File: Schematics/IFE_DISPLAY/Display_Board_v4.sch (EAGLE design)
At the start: 38 parts, among them J1 POWER_JACKPTH

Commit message: Display v4 - Routing
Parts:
- added R11, R4, R6: 23k, rcl:R-US_R0603
- added U$12: MC34063AD, Display_Custom:MC34063AD
- J1: value POWER_JACKPTH -> 5.5x2.1mm Barrel; device SparkFun-Connectors:POWER_JACKPTH -> SparkFun-Connectors:POWER_JACKSMD
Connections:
- net ~CS_CAN renamed !CS_CAN
- net ~INT_CAN renamed !INT_CAN
- new net !A_CS: ATMEGA328P.PD5, U$7.LOAD/CSN
- new net !B_CS: ATMEGA328P.PD4, U$8.LOAD/CSN
- new net !C_CS: ATMEGA328P.PD3, U$9.LOAD/CSN
- new net A_0: U$1.DIG_0, U$7.DIG_0
- new net A_1: U$1.DIG_1, U$7.DIG_1
- new net A_2: U$1.DIG_2, U$7.DIG_2
- new net A_3: U$1.DIG_3, U$7.DIG_3
- new net A_A: U$1.A, U$7.S_0
- new net A_B: U$1.B, U$7.S_1
- new net A_C: U$1.C, U$7.S_2
- new net A_D: U$1.D, U$7.S_3
- new net A_DP: U$1.DP, U$7.S_7
- new net A_E: U$1.E, U$7.S_4
- new net A_F: U$1.F, U$7.S_5
- new net A_G: U$1.G, U$7.S_6
- new net B_0: U$5.DIG_0, U$8.DIG_0
- new net B_1: U$5.DIG_1, U$8.DIG_1
- new net B_2: U$5.DIG_2, U$8.DIG_2
- new net B_3: U$5.DIG_3, U$8.DIG_3
- new net B_A: U$5.A, U$8.S_0
- new net B_B: U$5.B, U$8.S_1
- new net B_C: U$5.C, U$8.S_2
- new net B_D: U$5.D, U$8.S_3
- new net B_DP: U$5.DP, U$8.S_7
- new net B_E: U$5.E, U$8.S_4
- new net B_F: U$5.F, U$8.S_5
- new net B_G: U$5.G, U$8.S_6
- new net C_0: U$6.DIG_0, U$9.DIG_0
- new net C_1: U$6.DIG_1, U$9.DIG_1
- new net C_2: U$6.DIG_2, U$9.DIG_2
- new net C_3: U$6.DIG_3, U$9.DIG_3
- new net C_A: U$6.A, U$9.S_0
- new net C_B: U$6.B, U$9.S_1
- new net C_C: U$6.C, U$9.S_2
- new net C_D: U$6.D, U$9.S_3
- new net C_DP: U$6.DP, U$9.S_7
- new net C_E: U$6.E, U$9.S_4
- new net C_F: U$6.F, U$9.S_5
- new net C_G: U$6.G, U$9.S_6
- new net N$15: R6.1, U$8.ISET
- new net N$19: R11.1, U$9.ISET
- new net N$22: R4.1, U$7.ISET
- net +5V: now also R11.2, R4.2, R6.2, U$7.VDD, U$8.VDD, U$9.VDD
- net GND: now also U$12.A, U$7.GND, U$8.GND, U$9.GND
- net MISO: now also U$7.DOUT, U$8.DOUT, U$9.DOUT
- net MOSI: now also U$7.DIN, U$8.DIN, U$9.DIN
- net N$8: now also U$12.C
- net SCK: now also U$7.CLK, U$8.CLK, U$9.CLK

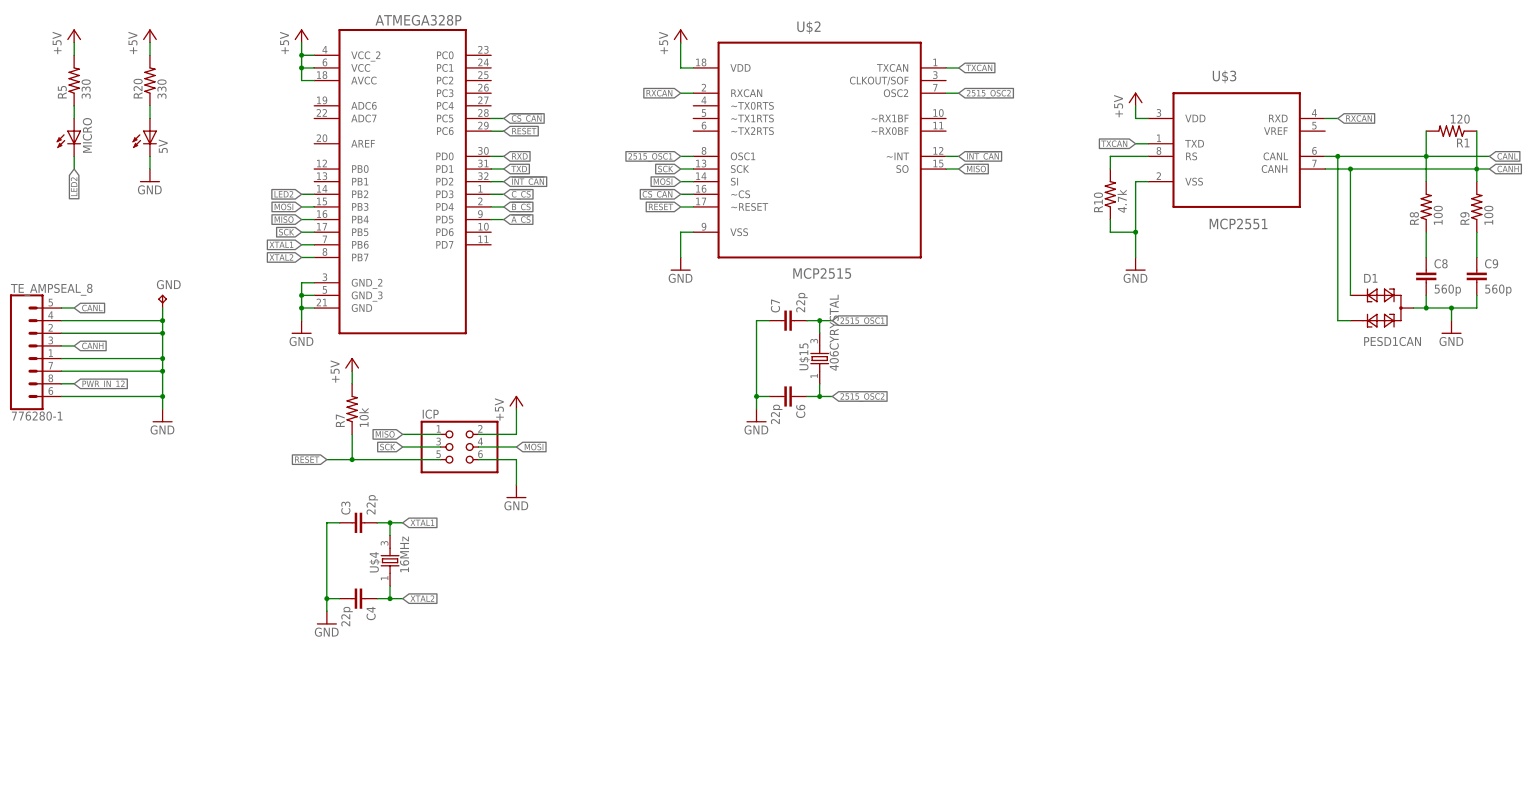
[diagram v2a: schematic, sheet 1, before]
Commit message: Display v4 - Adding FTDI for ease of programming
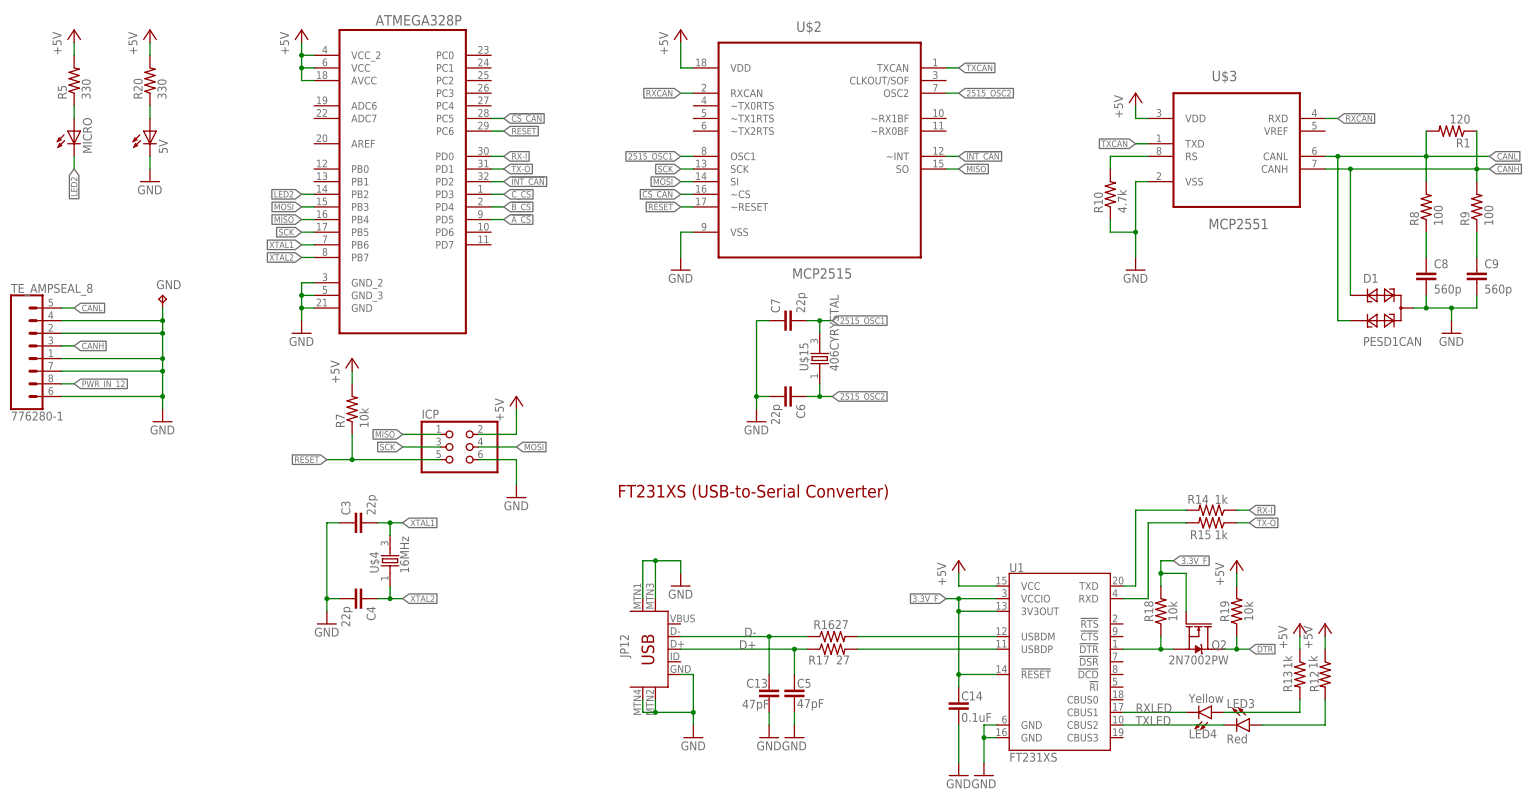
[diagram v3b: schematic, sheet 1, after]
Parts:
- added C13, C5: 47pF, SparkFun-Capacitors:47PF-0603-50V-5%
- added C14: 0.1uF, SparkFun-Capacitors:0.1UF-0603-25V-(+80/-20%)
- added JP12: USB-MINIB-5PIN, SparkFun-Connectors:USB-MINIB-5PIN
- added LED3: Red, SparkFun-LED:LED1206
- added LED4: Yellow, SparkFun-LED:LED1206
- added Q2: 2N7002PW, SparkFun-DiscreteSemi:MOSFET-NCH-2N7002PW
- added R12, R13, R14, R15: 1k, SparkFun-Resistors:1KOHM-0603-1/10W-1%
- added R16, R17: 27, SparkFun-Resistors:27OHM-0603-1/10W-1%
- added R18, R19: 10k, SparkFun-Resistors:10KOHM-0603-1/10W-1%
- added U1: FT231XS, SparkFun-IC-Comms:FT231XS
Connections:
- removed net RXD: ATMEGA328P.PD0
- removed net TXD: ATMEGA328P.PD1
- new net 3.3V_F: C14.1, Q2.G, R18.2, U1.!RESET, U1.3V3OUT, U1.VCCIO
- new net D+: C5.1, JP12.D+, R17.1
- new net D-: C13.1, JP12.D-, R16.1
- new net DTR: Q2.D, R19.1
- new net FTDI_DTR: Q2.S, R18.1, U1.!DTR
- new net N$1: LED3.A, R12.2
- new net N$10: LED4.A, R13.2
- new net N$2: R16.2, U1.USBDM
- new net N$4: R17.2, U1.USBDP
- new net RX-I: ATMEGA328P.PD0, R14.1
- new net RXD1: R15.2, U1.RXD
- new net RXLED: LED4.C, U1.CBUS1
- new net TX-O: ATMEGA328P.PD1, R15.1
- new net TXD1: R14.2, U1.TXD
- new net TXLED: LED3.C, U1.CBUS2
- net +5V: now also R12.1, R13.1, R19.2, U1.VCC
- net GND: now also C13.2, C14.2, C5.2, JP12.GND, JP12.MTN1, JP12.MTN2, JP12.MTN3, JP12.MTN4, U1.GND@16, U1.GND@6
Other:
- note added: "FT231XS (USB-to-Serial Converter)"

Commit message: v4 Ready to be printed
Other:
- note removed: "FT231XS (USB-to-Serial Converter)"
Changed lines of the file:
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@@
 <description>&lt;h3&gt;Micro and CAN&lt;/h3&gt;</description>
 <plain>
-<text x="129.54" y="33.02" size="2.54" layer="94" font="vector" ratio="15">FT231XS (USB-to-Serial Converter)</text>
 </plain>
 <instances>

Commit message: added BOM
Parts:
- added C10: 0.1u, resistor:C-EUC0805K
- C1: value 680u -> 220u
- C2: value 220u -> 680u
- renumbered LED3 to TX, LED4 to RX
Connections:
- net DTR: now also C10.2
- net RESET: now also C10.1
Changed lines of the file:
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@@
 <part name="U$10" library="Display_Custom" deviceset="LM2576D2T-ADJ" device=""/>
 <part name="U$11" library="Display_Custom" deviceset="INDUCTOR" device="" value="100uH"/>
-<part name="C1" library="rcl" library_urn="urn:adsk.eagle:library:334" deviceset="CPOL-US" device="UD-6,3X7,7" package3d_urn="urn:adsk.eagle:package:23472/1" value="680u"/>
-<part name="C2" library="rcl" library_urn="urn:adsk.eagle:library:334" deviceset="CPOL-US" device="UD-6,3X7,7" package3d_urn="urn:adsk.eagle:package:23472/1" value="220u"/>
+<part name="C1" library="rcl" library_urn="urn:adsk.eagle:library:334" deviceset="CPOL-US" device="UD-6,3X7,7" package3d_urn="urn:adsk.eagle:package:23472/1" value="220u"/>
+<part name="C2" library="rcl" library_urn="urn:adsk.eagle:library:334" deviceset="CPOL-US" device="UD-6,3X7,7" package3d_urn="urn:adsk.eagle:package:23472/1" value="680u"/>
 <part name="P+1" library="supply1" library_urn="urn:adsk.eagle:library:371" deviceset="V+" device=""/>
 <part name="P+2" library="supply1" library_urn="urn:adsk.eagle:library:371" deviceset="+5V" device=""/>
@@
 <part name="GND14" library="SparkFun-Aesthetics" deviceset="GND" device=""/>
 <part name="GND22" library="SparkFun-Aesthetics" deviceset="GND" device=""/>
-<part name="LED4" library="SparkFun-LED" deviceset="LED" device="1206" value="Yellow">
+<part name="RX" library="SparkFun-LED" deviceset="LED" device="1206" value="Yellow">
 <attribute name="PROD_ID" value="DIO-09909"/>
 </part>
-<part name="LED3" library="SparkFun-LED" deviceset="LED" device="1206" value="Red">
+<part name="TX" library="SparkFun-LED" deviceset="LED" device="1206" value="Red">
 <attribute name="PROD_ID" value="DIO-09912"/>
 </part>
@@
 <part name="P+8" library="supply1" deviceset="+5V" device=""/>
 <part name="P+10" library="supply1" deviceset="+5V" device=""/>
+<part name="C10" library="resistor" deviceset="C-EU" device="C0805K" value="0.1u"/>
 </parts>
 <sheets>
@@
 <instance part="GND14" gate="1" x="203.2" y="-22.86"/>
 <instance part="GND22" gate="1" x="198.12" y="-22.86"/>
-<instance part="LED4" gate="G$1" x="248.92" y="-10.16" rot="MR90">
+<instance part="RX" gate="G$1" x="248.92" y="-10.16" rot="MR90">
 <attribute name="PROD_ID" x="248.92" y="-10.16" size="1.778" layer="96" rot="MR90" display="off"/>
 </instance>
-<instance part="LED3" gate="G$1" x="256.54" y="-12.7" rot="R270">
+<instance part="TX" gate="G$1" x="256.54" y="-12.7" rot="R270">
 <attribute name="PROD_ID" x="256.54" y="-12.7" size="1.778" layer="96" rot="R270" display="off"/>
 </instance>
@@
 <instance part="P+8" gate="1" x="266.7" y="7.62"/>
 <instance part="P+10" gate="1" x="271.78" y="7.62"/>
+<instance part="C10" gate="G$1" x="68.58" y="48.26" rot="R180"/>
 </instances>
 <busses>
@@
 <pinref part="ICP" gate="A" pin="5"/>
 <wire x1="93.98" y1="40.64" x2="76.2" y2="40.64" width="0.1524" layer="91"/>
-<label x="71.12" y="40.64" size="1.27" layer="95" rot="R180" xref="yes"/>
+<label x="63.5" y="40.64" size="1.27" layer="95" rot="R180" xref="yes"/>
 <pinref part="R7" gate="G$1" pin="1"/>
-<wire x1="76.2" y1="40.64" x2="71.12" y2="40.64" width="0.1524" layer="91"/>
+<wire x1="76.2" y1="40.64" x2="68.58" y2="40.64" width="0.1524" layer="91"/>
+<wire x1="68.58" y1="40.64" x2="63.5" y2="40.64" width="0.1524" layer="91"/>
 <wire x1="76.2" y1="45.72" x2="76.2" y2="40.64" width="0.1524" layer="91"/>
 <junction x="76.2" y="40.64"/>
+<pinref part="C10" gate="G$1" pin="1"/>
+<wire x1="68.58" y1="45.72" x2="68.58" y2="40.64" width="0.1524" layer="91"/>
+<junction x="68.58" y="40.64"/>
 </segment>
 <segment>
@@
 <label x="256.54" y="2.54" size="1.27" layer="95" font="vector" xref="yes"/>
 </segment>
+<segment>
+<pinref part="C10" gate="G$1" pin="2"/>
+<wire x1="68.58" y1="58.42" x2="68.58" y2="53.34" width="0.1524" layer="91"/>
+<label x="68.58" y="58.42" size="1.27" layer="95" rot="R180" xref="yes"/>
+</segment>
 </net>
 <net name="D-" class="0">
@@
 <label x="233.68" y="-12.7" size="1.778" layer="95" font="vector"/>
 <pinref part="U1" gate="U$1" pin="CBUS2"/>
-<pinref part="LED3" gate="G$1" pin="C"/>
+<pinref part="TX" gate="G$1" pin="C"/>
 </segment>
 </net>
@@
 <wire x1="231.14" y1="-10.16" x2="243.84" y2="-10.16" width="0.1524" layer="91"/>
 <label x="233.68" y="-10.16" size="1.778" layer="95" font="vector"/>
-<pinref part="LED4" gate="G$1" pin="C"/>
+<pinref part="RX" gate="G$1" pin="C"/>
 </segment>
 </net>
@@
 <wire x1="271.78" y1="-7.62" x2="271.78" y2="-12.7" width="0.1524" layer="91"/>
 <wire x1="271.78" y1="-12.7" x2="259.08" y2="-12.7" width="0.1524" layer="91"/>
-<pinref part="LED3" gate="G$1" pin="A"/>
+<pinref part="TX" gate="G$1" pin="A"/>
 </segment>
 </net>
@@
 <wire x1="266.7" y1="-7.62" x2="266.7" y2="-10.16" width="0.1524" layer="91"/>
 <wire x1="266.7" y1="-10.16" x2="251.46" y2="-10.16" width="0.1524" layer="91"/>
-<pinref part="LED4" gate="G$1" pin="A"/>
-</segment>
-</net>
+<pinref part="RX" gate="G$1" pin="A"/>
+</segment>
+</net>

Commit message: Added 2 new power relays
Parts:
- C3, C4, C6, C7: value 22p -> 18p
- R12, R13: value 1k -> 330
- RX: value Yellow -> RED
- TX: value Red -> RED
- U$15: value 406CYRYSTAL -> 16MHz
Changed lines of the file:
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@@
 <part name="MICRO" library="led" deviceset="LED" device="CHIP-LED0805"/>
 <part name="R5" library="resistor" deviceset="R-US_" device="R0805" value="330"/>
-<part name="C3" library="resistor" deviceset="C-EU" device="C0805K" value="22p"/>
-<part name="C4" library="resistor" deviceset="C-EU" device="C0805K" value="22p"/>
+<part name="C3" library="resistor" deviceset="C-EU" device="C0805K" value="18p"/>
+<part name="C4" library="resistor" deviceset="C-EU" device="C0805K" value="18p"/>
 <part name="GND8" library="supply1" deviceset="GND" device=""/>
 <part name="ICP" library="pinhead" deviceset="PINHD-2X3" device=""/>
@@
 <part name="GND9" library="supply1" deviceset="GND" device=""/>
 <part name="U$2" library="Microchip_By_element14_Batch_1" deviceset="MCP2515-I/SO" device="" value="MCP2515"/>
-<part name="C6" library="resistor" deviceset="C-EU" device="C0805K" value="22p"/>
-<part name="C7" library="resistor" deviceset="C-EU" device="C0805K" value="22p"/>
+<part name="C6" library="resistor" deviceset="C-EU" device="C0805K" value="18p"/>
+<part name="C7" library="resistor" deviceset="C-EU" device="C0805K" value="18p"/>
 <part name="GND16" library="supply1" deviceset="GND" device=""/>
 <part name="P+19" library="supply1" deviceset="+5V" device=""/>
@@
 <part name="GND" library="testpad" library_urn="urn:adsk.eagle:library:385" deviceset="TP" device="TP12SQ" package3d_urn="urn:adsk.eagle:package:27964/1"/>
 <part name="U$4" library="Display_Custom" deviceset="406CYRYSTAL" device="" value="16MHz"/>
-<part name="U$15" library="Display_Custom" deviceset="406CYRYSTAL" device=""/>
+<part name="U$15" library="Display_Custom" deviceset="406CYRYSTAL" device="" value="16MHz"/>
 <part name="FRAME1" library="frames" library_urn="urn:adsk.eagle:library:229" deviceset="LETTER_L" device=""/>
 <part name="FRAME2" library="frames" library_urn="urn:adsk.eagle:library:229" deviceset="LETTER_L" device=""/>
@@
 <part name="U$6" library="Display_Custom" deviceset="LDQ-N516RI" device=""/>
 <part name="GND11" library="SparkFun-Aesthetics" deviceset="GND" device=""/>
-<part name="R12" library="SparkFun-Resistors" deviceset="1KOHM" device="-0603-1/10W-1%" value="1k"/>
-<part name="R13" library="SparkFun-Resistors" deviceset="1KOHM" device="-0603-1/10W-1%" value="1k"/>
+<part name="R12" library="SparkFun-Resistors" deviceset="1KOHM" device="-0603-1/10W-1%" value="330"/>
+<part name="R13" library="SparkFun-Resistors" deviceset="1KOHM" device="-0603-1/10W-1%" value="330"/>
 <part name="R14" library="SparkFun-Resistors" deviceset="1KOHM" device="-0603-1/10W-1%" value="1k"/>
 <part name="R15" library="SparkFun-Resistors" deviceset="1KOHM" device="-0603-1/10W-1%" value="1k"/>
@@
 <part name="GND14" library="SparkFun-Aesthetics" deviceset="GND" device=""/>
 <part name="GND22" library="SparkFun-Aesthetics" deviceset="GND" device=""/>
-<part name="RX" library="SparkFun-LED" deviceset="LED" device="1206" value="Yellow">
+<part name="RX" library="SparkFun-LED" deviceset="LED" device="1206" value="RED">
 <attribute name="PROD_ID" value="DIO-09909"/>
 </part>
-<part name="TX" library="SparkFun-LED" deviceset="LED" device="1206" value="Red">
+<part name="TX" library="SparkFun-LED" deviceset="LED" device="1206" value="RED">
 <attribute name="PROD_ID" value="DIO-09912"/>
 </part>
